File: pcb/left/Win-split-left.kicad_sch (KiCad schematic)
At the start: 158 parts, among them J1 Conn_01x04_Socket, Q1 Q_PMOS_GSD, SW8 ROT_SKYLOONG_HS, U1 RP2040_ProMicro, U3 74AHCT1G125

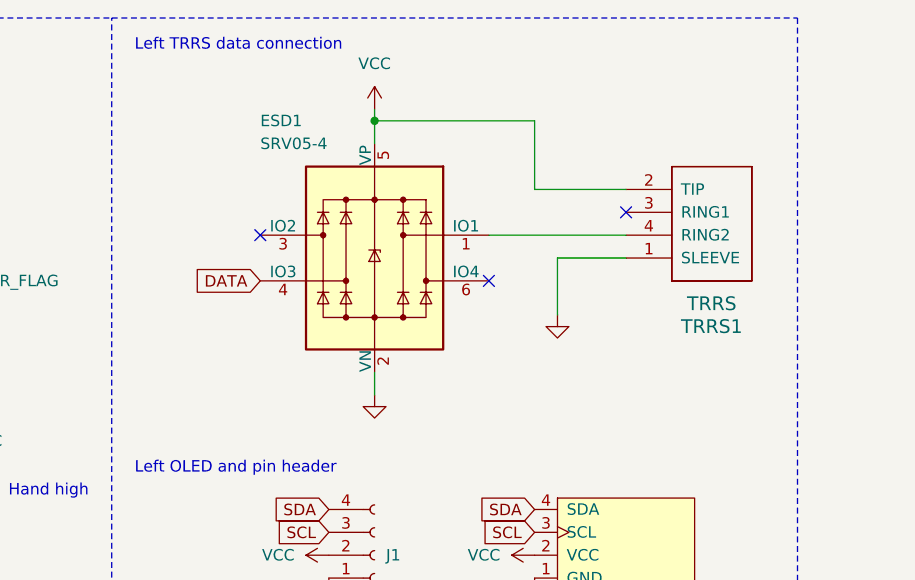
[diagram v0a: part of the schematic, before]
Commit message: vial firmware and 3D cases
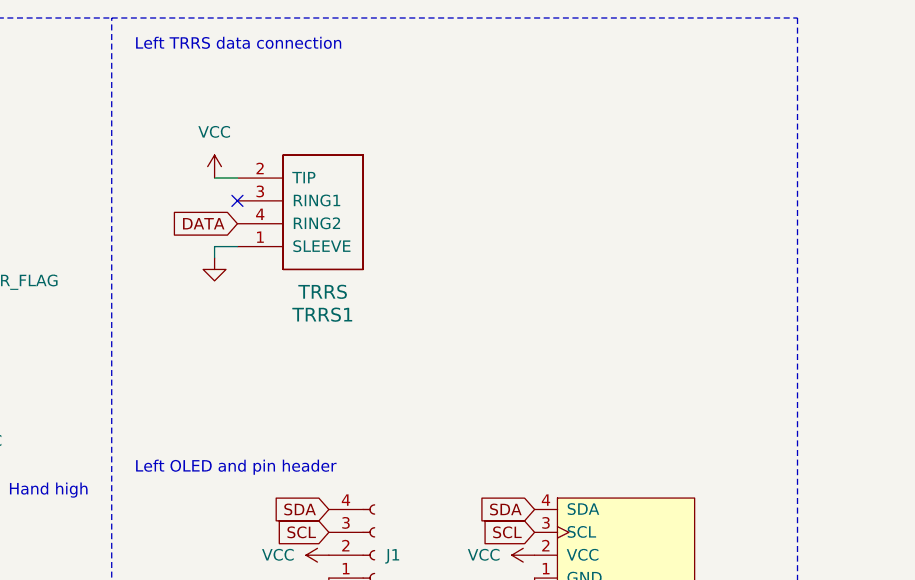
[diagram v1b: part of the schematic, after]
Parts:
- removed ESD1: SRV05-4, PCM_marbastlib-various:SOT-23-6-routable, symbol PCM_marbastlib-various:SRV05-4
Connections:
- net DATA: now also TRRS1.4 (RING2)
- no-connect marks 14 -> 12
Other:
- moved on the sheet: TRRS1
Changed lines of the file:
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@@
   (junction (at 243.84 383.54) (diameter 0) (color 0 0 0 0)
   )
-  (junction (at 116.84 26.67) (diameter 0) (color 0 0 0 0)
-  )
   (junction (at 134.62 177.8) (diameter 0) (color 0 0 0 0)
   )
@@
   (junction (at 193.04 461.01) (diameter 0) (color 0 0 0 0)
   )
-  (no_connect (at 129.54 44.45))
   (no_connect (at 43.18 34.29))
-  (no_connect (at 104.14 39.37))
   (no_connect (at 35.56 49.53))
   (no_connect (at 60.96 36.83))
   (no_connect (at 55.88 71.12))
-  (no_connect (at 144.78 36.83))
+  (no_connect (at 101.6 35.56))
   (no_connect (at 40.64 71.12))
   (no_connect (at 35.56 36.83))
@@
     (stroke (width 0) (type default))
   )
-  (wire (pts (xy 134.62 26.67) (xy 116.84 26.67))
-    (stroke (width 0) (type default))
-  )
   (wire (pts (xy 116.84 411.48) (xy 116.84 414.02))
     (stroke (width 0) (type default))
@@
     (stroke (width 0) (type default))
   )
-  (wire (pts (xy 116.84 26.67) (xy 116.84 29.21))
-    (stroke (width 0) (type default))
-  )
   (wire (pts (xy 269.24 497.84) (xy 269.24 505.46))
     (stroke (width 0) (type default))
@@
     (stroke (width 0) (type default))
   )
-  (wire (pts (xy 129.54 39.37) (xy 144.78 39.37))
-    (stroke (width 0) (type default))
-  )
   (polyline (pts (xy 87.63 15.24) (xy 163.83 15.24))
     (stroke (width 0) (type dash_dot))
@@
     (stroke (width 0) (type default))
   )
-  (wire (pts (xy 144.78 41.91) (xy 137.16 41.91))
+  (wire (pts (xy 101.6 40.64) (xy 99.06 40.64))
     (stroke (width 0) (type default))
   )
@@
     (stroke (width 0) (type default))
   )
-  (wire (pts (xy 116.84 54.61) (xy 116.84 57.15))
-    (stroke (width 0) (type default))
-  )
   (wire (pts (xy 60.96 67.31) (xy 63.5 67.31))
     (stroke (width 0) (type default))
@@
     (stroke (width 0) (type default))
   )
-  (wire (pts (xy 134.62 34.29) (xy 144.78 34.29))
-    (stroke (width 0) (type default))
-  )
   (wire (pts (xy 116.84 436.88) (xy 137.16 436.88))
     (stroke (width 0) (type default))
@@
     (stroke (width 0) (type default))
   )
-  (wire (pts (xy 134.62 34.29) (xy 134.62 26.67))
-    (stroke (width 0) (type default))
-  )
   (wire (pts (xy 278.13 406.4) (xy 292.1 406.4))
     (stroke (width 0) (type default))
@@
     (stroke (width 0) (type default))
   )
-  (wire (pts (xy 116.84 25.4) (xy 116.84 26.67))
-    (stroke (width 0) (type default))
-  )
   (polyline (pts (xy 15.24 15.24) (xy 15.24 83.82))
     (stroke (width 0) (type dash_dot))
@@
     (stroke (width 0) (type dash_dot))
   )
-  (wire (pts (xy 137.16 41.91) (xy 137.16 48.26))
+  (wire (pts (xy 99.06 40.64) (xy 99.06 41.91))
     (stroke (width 0) (type default))
   )
@@
     (stroke (width 0) (type default))
   )
+  (wire (pts (xy 99.06 33.02) (xy 101.6 33.02))
+    (stroke (width 0) (type default))
+  )
   (wire (pts (xy 269.24 383.54) (xy 243.84 383.54))
     (stroke (width 0) (type default))
@@
     )
   )
-  (global_label "DATA" (shape input) (at 104.14 44.45 180) (fields_autoplaced)
-    (effects (font (size 1.27 1.27)) (justify right))
-    (property "Intersheetrefs" "${INTERSHEET_REFS}" (at 96.74 44.45 0)
-      (effects (font (size 1.27 1.27)) (justify right) hide)
-    )
-  )
   (global_label "ROW0" (shape input) (at 60.96 54.61 0) (fields_autoplaced)
     (effects (font (size 1.27 1.27)) (justify left))
@@
     )
   )
+  (global_label "DATA" (shape input) (at 101.6 38.1 180) (fields_autoplaced)
+    (effects (font (size 1.27 1.27)) (justify right))
+    (property "Intersheetrefs" "${INTERSHEET_REFS}" (at 94.2 38.1 0)
+      (effects (font (size 1.27 1.27)) (justify right) hide)
+    )
+  )
   (global_label "ROTA" (shape input) (at 53.34 71.12 270) (fields_autoplaced)
     (effects (font (size 1.27 1.27)) (justify right))
@@
     )
   )
-  (symbol (lib_id "ScottoKeebs:Placeholder_TRRS") (at 153.67 44.45 0) (unit 1)
+  (symbol (lib_id "ScottoKeebs:Placeholder_TRRS") (at 110.49 43.18 0) (unit 1)
     (in_bom yes) (on_board yes) (dnp no)
-    (property "Reference" "TRRS1" (at 154.305 49.53 0)
+    (property "Reference" "TRRS1" (at 111.125 48.26 0)
       (effects (font (size 1.524 1.524)))
     )
-    (property "Value" "TRRS" (at 154.305 46.99 0)
+    (property "Value" "TRRS" (at 111.125 45.72 0)
       (effects (font (size 1.524 1.524)))
     )
-    (property "Footprint" "ScottoKeebs_Components:TRRS_PJ-320A" (at 157.48 44.45 0)
+    (property "Footprint" "ScottoKeebs_Components:TRRS_PJ-320A" (at 114.3 43.18 0)
       (effects (font (size 1.524 1.524)) hide)
     )
-    (property "Datasheet" "" (at 157.48 44.45 0)
+    (property "Datasheet" "" (at 114.3 43.18 0)
       (effects (font (size 1.524 1.524)) hide)
     )
@@
     )
   )
-  (symbol (lib_name "GND_2") (lib_id "power:GND") (at 137.16 48.26 0) (mirror y) (unit 1)
+  (symbol (lib_name "GND_2") (lib_id "power:GND") (at 99.06 41.91 0) (mirror y) (unit 1)
     (in_bom yes) (on_board yes) (dnp no) (fields_autoplaced)
-    (property "Reference" "#PWR013" (at 137.16 54.61 0)
+    (property "Reference" "#PWR013" (at 99.06 48.26 0)
       (effects (font (size 1.27 1.27)) hide)
     )
-    (property "Value" "GND" (at 137.16 52.07 90)
+    (property "Value" "GND" (at 99.06 45.72 90)
       (effects (font (size 1.27 1.27)) (justify right) hide)
     )
-    (property "Footprint" "" (at 137.16 48.26 0)
+    (property "Footprint" "" (at 99.06 41.91 0)
       (effects (font (size 1.27 1.27)) hide)
     )
-    (property "Datasheet" "" (at 137.16 48.26 0)
+    (property "Datasheet" "" (at 99.06 41.91 0)
       (effects (font (size 1.27 1.27)) hide)
     )
@@
     )
   )
-  (symbol (lib_id "power:VCC") (at 116.84 25.4 0) (mirror y) (unit 1)
+  (symbol (lib_id "power:VCC") (at 99.06 33.02 0) (mirror y) (unit 1)
     (in_bom yes) (on_board yes) (dnp no) (fields_autoplaced)
-    (property "Reference" "#PWR014" (at 116.84 29.21 0)
+    (property "Reference" "#PWR014" (at 99.06 36.83 0)
       (effects (font (size 1.27 1.27)) hide)
     )
-    (property "Value" "VCC" (at 116.84 20.32 0)
+    (property "Value" "VCC" (at 99.06 27.94 0)
       (effects (font (size 1.27 1.27)))
     )
-    (property "Footprint" "" (at 116.84 25.4 0)
+    (property "Footprint" "" (at 99.06 33.02 0)
       (effects (font (size 1.27 1.27)) hide)
     )
-    (property "Datasheet" "" (at 116.84 25.4 0)
+    (property "Datasheet" "" (at 99.06 33.02 0)
       (effects (font (size 1.27 1.27)) hide)
     )
@@
     )
   )
-  (symbol (lib_id "PCM_marbastlib-various:SRV05-4") (at 116.84 41.91 0) (mirror y) (unit 1)
-    (in_bom yes) (on_board yes) (dnp no)
-    (property "Reference" "ESD1" (at 104.14 26.67 0)
-      (effects (font (size 1.27 1.27)) (justify right))
-    )
-    (property "Value" "SRV05-4" (at 104.14 29.21 0)
-      (effects (font (size 1.27 1.27)) (justify right))
-    )
-    (property "Footprint" "PCM_marbastlib-various:SOT-23-6-routable" (at 99.06 53.34 0)
-      (effects (font (size 1.27 1.27)) hide)
-    )
-    (property "Datasheet" "http://www.onsemi.com/pub/Collateral/SRV05-4-D.PDF" (at 116.84 41.91 0)
-      (effects (font (size 1.27 1.27)) hide)
-    )
-    (property "LCSC" "C558418" (at 116.84 41.91 0)
-      (effects (font (size 1.27 1.27)) hide)
-    )
-    (pin "1")
-    (pin "2")
-    (pin "3")
-    (pin "4")
-    (pin "5")
-    (pin "6")
-    (instances
-      (project "Win-split-left"
-        (path "/49098896-502f-4162-bad5-517f7d921ed4"
-          (reference "ESD1") (unit 1)
-        )
-      )
-    )
-  )
   (symbol (lib_id "PCM_marbastlib-mx:MX_SK6812MINI-E") (at 278.13 421.64 0) (unit 1)
     (in_bom yes) (on_board yes) (dnp no)
@@
         )
       )
-    )
-  )
-  (symbol (lib_id "power:GND") (at 116.84 57.15 0) (mirror y) (unit 1)
-    (in_bom yes) (on_board yes) (dnp no)
-    (property "Reference" "#PWR011" (at 116.84 63.5 0)
-      (effects (font (size 1.27 1.27)) hide)
-    )
-    (property "Value" "GND" (at 116.713 61.5442 0)
-      (effects (font (size 1.27 1.27)) hide)
-    )
-    (property "Footprint" "" (at 116.84 57.15 0)
-      (effects (font (size 1.27 1.27)) hide)
-    )
-    (property "Datasheet" "" (at 116.84 57.15 0)
-      (effects (font (size 1.27 1.27)) hide)
-    )
-    (pin "1")
-    (instances
-      (project "Lotus58_Glow_140"
-        (path "/033c564d-3d11-4dc7-8633-0c6732489a73"
-          (reference "#PWR011") (unit 1)
-        )
-      )
-      (project "Win-split-left"
-        (path "/49098896-502f-4162-bad5-517f7d921ed4"
-          (reference "#PWR021") (unit 1)
-        )
-      )
